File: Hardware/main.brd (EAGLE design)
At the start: 78.7 x 49.2 mm, 26 parts, among them IC3 MEGA128-A, K1 DS2-L2-12V, T1 IRML5202, T2 IRML5202, T3 IRML5202

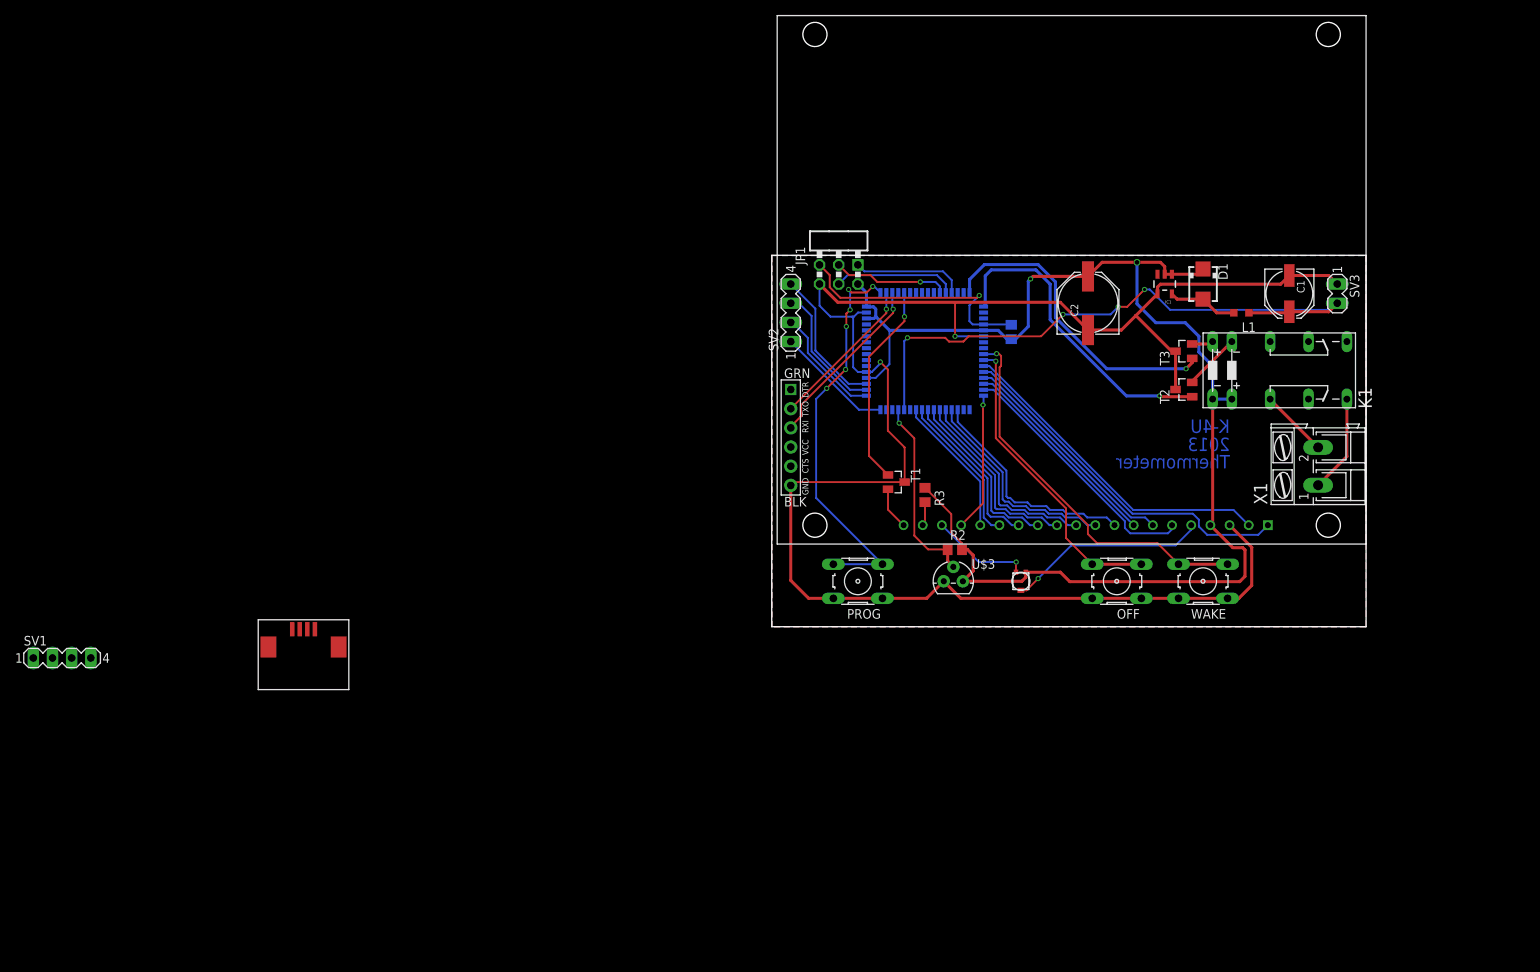
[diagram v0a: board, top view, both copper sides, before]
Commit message: Added a ds1307
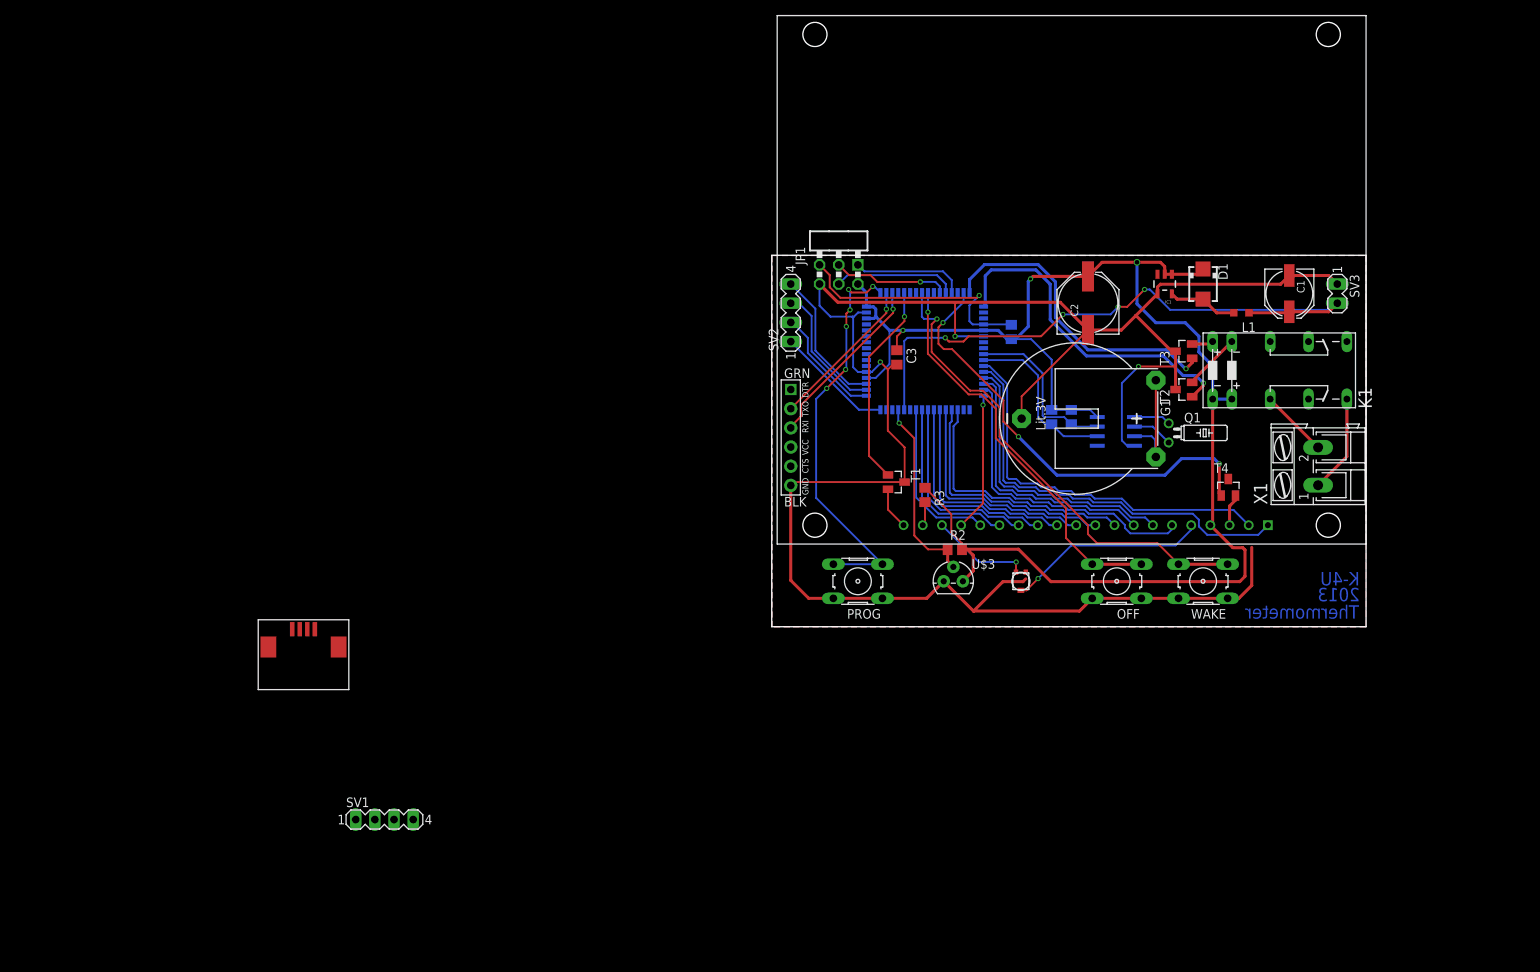
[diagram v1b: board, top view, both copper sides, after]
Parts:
- added C3: (no value), rcl:C0805
- added G1: CR2032H, battery:CR2032H
- added Q1: (no value), crystal:TC26H
- added R5, R6: 10K, rcl:R0805
- added T4: IRML5202, custom:SOT23
- added U1: DS1307ZN+, custom:SOIC127P600X175-8N
- moved SV1 47.8 mm to (-51.3, -25.2)
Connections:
- new net DISPLAY: IC3.15, T4.1
- new net N$23: T4.2, U$2.P$3
- new net N$24: G1.+, G1.+@1, U1.3
- new net N$26: Q1.1, U1.1
- new net N$27: Q1.2, U1.2
- new net SCL: IC3.25, R5.1, U1.7
- new net SDA: IC3.26, R6.1, U1.6
- net +5V: now also C3.1, R5.2, R6.2, U1.8; no longer R4.1
- net GND: now also C3.2, G1.-, R4.1, T4.3, U1.4; no longer U$2.P$3
- net N$10: now also IC3.8; no longer IC3.25
- net N$16: now also IC3.9; no longer IC3.26
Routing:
- net DISPLAY: track 0.00 -> 59.7 mm, vias 0 -> 3
- net GND: track 235.8 -> 276.2 mm, vias 2 -> 3
- net +5V: track 177.7 -> 200.7 mm, vias 2 -> 3
- net SDA: track 0.00 -> 22.5 mm
- net SCL: track 0.00 -> 22.3 mm
- net N$24: track 0.00 -> 15.4 mm
- net N$10: track 51.2 -> 63.8 mm
- net N$16: track 40.4 -> 52.5 mm
- net E: track 27.6 -> 35.3 mm
- net R/W: track 30.5 -> 37.9 mm
- net CS1: track 47.7 -> 55.1 mm
- net CS2: track 43.9 -> 51.1 mm
- net D/I: track 34.1 -> 41.1 mm
- net N$27: track 0.00 -> 5.41 mm
- net N$26: track 0.00 -> 4.88 mm
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
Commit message: Rotated the PCB, Added a button + LED
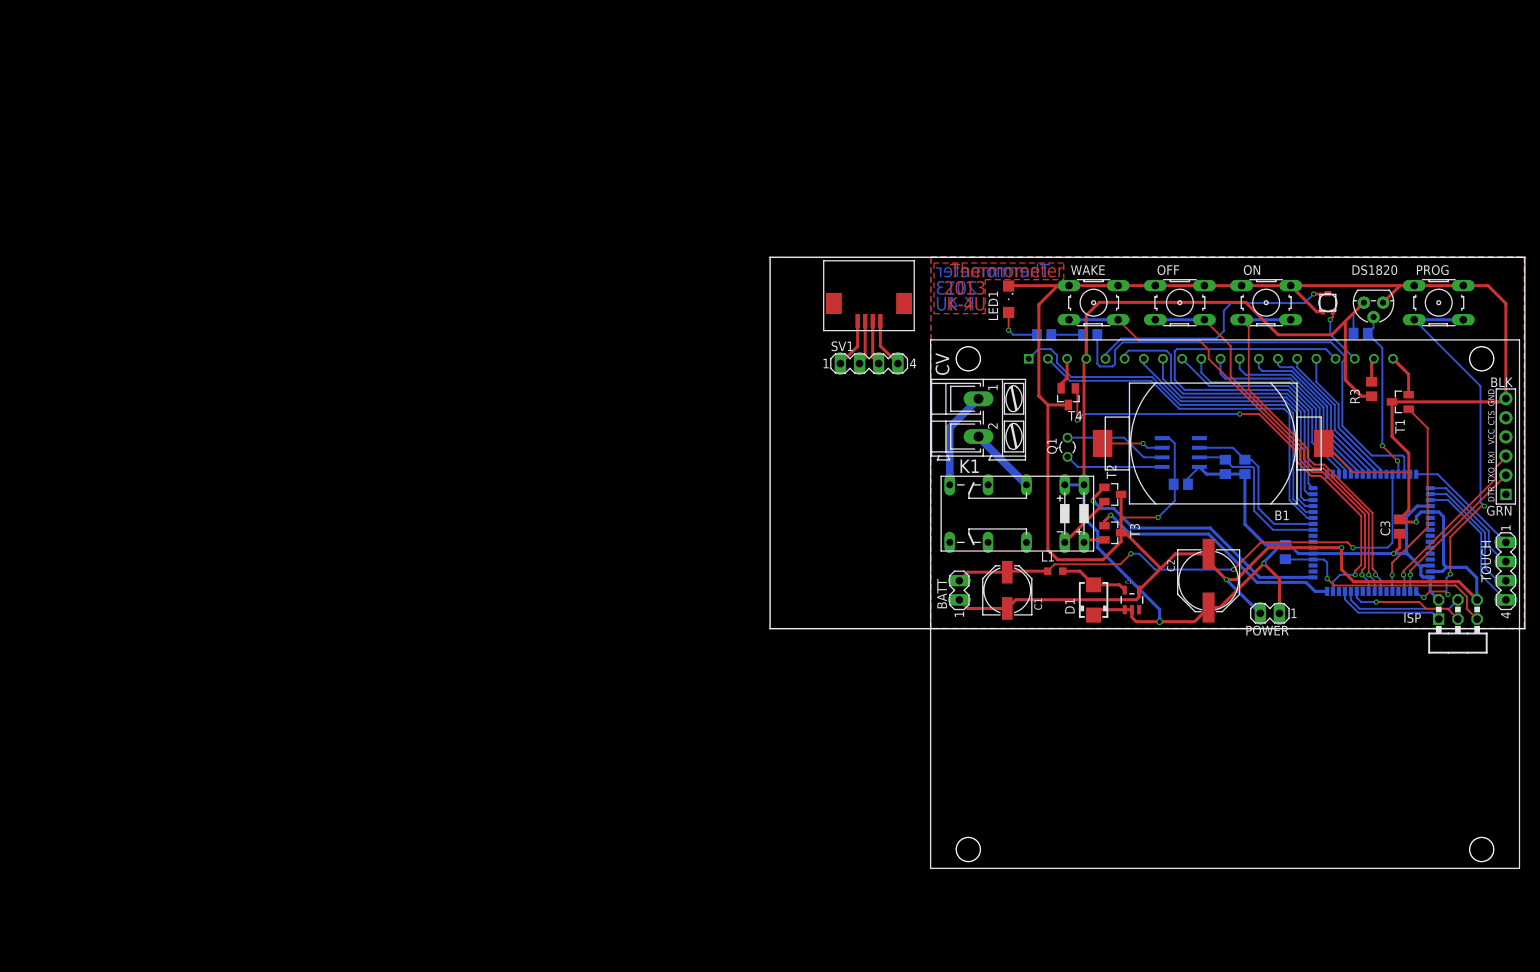
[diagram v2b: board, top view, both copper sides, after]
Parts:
- removed G1: CR2032H, battery:CR2032H
- removed JP1: AVR-ISP-6HORZ, avr-7:AVR-ISP-6R
- removed SV2: (no value), con-lstb:MA04-1
- removed SV3: (no value), con-lstb:MA02-1
- removed U$3: DS18B20, joep-custom:TO92
- removed X1: (no value), con-ptr500:AK300/2
- added B1: CR2032MULTICOMP, custom:CR2032
- added BATT, POWER: (no value), con-lstb:MA02-1
- added C4: (no value), rcl:C0805
- added CV: (no value), con-ptr500:AK300/2
- added DS1820: DS18B20, joep-custom:TO92
- added ISP: AVR-ISP-6HORZ, avr-7:AVR-ISP-6R
- added LED1: (no value), led:SML1206
- added ON: (no value), switch-omron:B3F-10XX
- added R7, R8: 150, rcl:R0805
- added TOUCH: (no value), con-lstb:MA04-1
- Q1: device crystal:TC26H -> crystal:TC26V
- moved U$2 126.8 mm to (21.1, -31.7), turned to 0 degrees
- moved JP2 94.7 mm to (97.3, 24.2), turned to 90 degrees
- moved SV1 88.1 mm to (12.9, 35.2)
- moved U$1 87.9 mm to (14.4, 40.8), turned to 180 degrees
- moved PROG 85.3 mm to (88.4, 43.2), turned to 0 degrees
- moved C3 70.3 mm to (83.2, 13.6), turned to 90 degrees
- moved T1 67.6 mm to (83.3, 30.1), turned to 90 degrees
- moved IC3 63.9 mm to (79.5, 12.8), turned to 90 degrees
- moved R2 60.9 mm to (78.0, 39.2), flipped to the bottom
- moved R3 60.8 mm to (79.5, 31.8), turned to 90 degrees
- moved R4 54.9 mm to (73.7, 43.2), turned to 0 degrees
- moved C1 54.2 mm to (31.2, 5.15), turned to 90 degrees
- moved R1 46.5 mm to (68.0, 10.2), turned to 270 degrees
- moved D1 44.3 mm to (42.6, 3.88), turned to 90 degrees
- moved L1 42.2 mm to (37.6, 7.69), turned to 0 degrees
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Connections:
- new net N$28: IC3.7, ON.3, ON.4
- new net N$29: LED1.A, R8.2
- new net N$30: IC3.46, R7.1
- new net N$31: R7.2, R8.1
- net !RESET: now also ISP.5; no longer JP1.5
- net +5V: now also C4.1, DS1820.3, ISP.2, POWER.1; no longer JP1.2, U$3.3
- net DS18B20: now also DS1820.2; no longer U$3.2
- net GND: now also B1.NEG, BATT.1, C4.2, DS1820.1, ISP.6, LED1.C, ON.1, ON.2, POWER.2; no longer G1.-, JP1.6, SV3.1, U$3.1
- net MISO: now also ISP.1; no longer JP1.1
- net MOSI: now also ISP.4; no longer JP1.4
- net N$10: now also IC3.9; no longer IC3.8
- net N$16: now also IC3.8; no longer IC3.9
- net N$17: now also CV.2; no longer X1.2
- net N$18: now also CV.1; no longer X1.1
- net N$19: now also TOUCH.4; no longer SV2.4
- net N$20: now also TOUCH.3; no longer SV2.3
- net N$21: now also TOUCH.2; no longer SV2.2
- net N$22: now also TOUCH.1; no longer SV2.1
- net N$24: now also B1.POS; no longer G1.+, G1.+@1
- net SCK: now also ISP.3; no longer JP1.3
- net V+: now also BATT.2; no longer SV3.2
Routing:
- net N$30: track 0.00 -> 61.5 mm
- net GND: track 276.2 -> 331.8 mm, vias 3 -> 4
- net N$28: track 0.00 -> 50.9 mm, vias 0 -> 1
- net RST: track 18.4 -> 55.7 mm, vias 1 -> 0
- net V+: track 83.4 -> 70.9 mm, vias 4 -> 3
- net R_S: track 44.8 -> 35.7 mm
- net N$13: track 26.5 -> 35.0 mm
- net N$27: track 5.41 -> 13.6 mm
- net N$26: track 4.88 -> 13.1 mm
- net N$24: track 15.4 -> 8.12 mm, vias 0 -> 1
- net R_R: track 41.4 -> 34.6 mm
- net N$3: track 0.00 -> 6.58 mm
- net N$6: track 0.00 -> 6.56 mm
- net N$29: track 0.00 -> 6.35 mm, vias 0 -> 1
- net N$4: track 0.00 -> 5.94 mm
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- added copper zone on layer 1, net N$32
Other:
- board size 78.7 x 49.2 mm -> 100 x 49.2 mm

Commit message: Partially working firmware. It's just a test
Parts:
- added R9: 10K, rcl:R0805
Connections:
- new net CV_ON: IC3.14, K1.S2, R9.2
- net +5V: now also K1.P2
- net GND: now also R9.1
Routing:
- net CV_ON: track 0.00 -> 56.8 mm, vias 0 -> 2
- net +5V: track 204.4 -> 213.5 mm
- net GND: track 331.8 -> 339.6 mm
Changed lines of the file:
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@@
 <element name="C4" library="rcl" package="C0805" value="" x="54.2" y="19.2" rot="MR0"/>
 <element name="POWER" library="con-lstb" package="MA02-1" value="" x="66" y="2.1" rot="R180"/>
+<element name="R9" library="rcl" package="R0805" value="10K" x="69.9" y="3.2" rot="MR90"/>
 </elements>
 <signals>
@@
 <wire x1="82.2359" y1="20.5297" x2="82.2359" y2="11.4359" width="0.254" layer="16"/>
 <wire x1="82.2359" y1="11.4359" x2="81.6" y2="10.8" width="0.254" layer="16"/>
-<via x="61.2" y="7.9" extent="1-16" drill="0.4"/>
-<wire x1="64.8" y1="11.5" x2="61.2" y2="7.9" width="0.254" layer="1"/>
-<wire x1="61.2" y1="7.9" x2="50.8" y2="7.9" width="0.254" layer="16"/>
-<wire x1="76.3" y1="11.5" x2="64.8" y2="11.5" width="0.254" layer="1"/>
-<wire x1="50.8" y1="7.9" x2="48.7" y2="10" width="0.254" layer="16"/>
+<wire x1="76.3" y1="11.5" x2="61.4" y2="11.5" width="0.254" layer="1"/>
 <wire x1="48.7" y1="10" x2="47.6" y2="10" width="0.254" layer="16"/>
 <via x="47.6" y="10" extent="1-16" drill="0.4"/>
@@
 <via x="77" y="10.8" extent="1-16" drill="0.4"/>
 <wire x1="77" y1="10.8" x2="81.6" y2="10.8" width="0.254" layer="16"/>
+<wire x1="48.7" y1="10" x2="50.2" y2="11.5" width="0.254" layer="16"/>
+<wire x1="50.2" y1="11.5" x2="55.5" y2="11.5" width="0.254" layer="16"/>
+<via x="55.5" y="11.5" extent="1-16" drill="0.4"/>
+<wire x1="55.5" y1="11.5" x2="57.2" y2="13.2" width="0.254" layer="1"/>
+<wire x1="57.2" y1="13.2" x2="59.7" y2="13.2" width="0.254" layer="1"/>
+<wire x1="59.7" y1="13.2" x2="61.4" y2="11.5" width="0.254" layer="1"/>
 </signal>
 <signal name="N$1">
@@
 <wire x1="77.1" y1="6.3" x2="91.03" y2="6.3" width="0.4064" layer="1"/>
 <wire x1="61.56" y1="6.56" x2="60.24" y2="6.56" width="0.4064" layer="1"/>
-<wire x1="59.45" y1="7.35" x2="58" y2="8.8" width="0.4064" layer="1"/>
+<wire x1="60.24" y1="6.56" x2="58" y2="8.8" width="0.4064" layer="1"/>
 <wire x1="58" y1="8.8" x2="58" y2="9.86" width="0.4064" layer="1"/>
 <wire x1="58" y1="9.86" x2="57.89" y2="9.97" width="0.4064" layer="1"/>
@@
 <wire x1="64.7" y1="2.1" x2="60.24" y2="6.56" width="0.4064" layer="16"/>
 <via x="60.24" y="6.56" extent="1-16" drill="0.4"/>
-<wire x1="60.24" y1="6.56" x2="59.45" y2="7.35" width="0.4064" layer="1"/>
+<contactref element="R9" pad="1"/>
+<wire x1="69.9" y1="2.25" x2="67.55" y2="4.6" width="0.254" layer="16"/>
+<wire x1="67.55" y1="4.6" x2="66.2" y2="4.6" width="0.254" layer="16"/>
+<wire x1="66.2" y1="4.6" x2="64.73" y2="3.13" width="0.254" layer="16"/>
+<wire x1="64.73" y1="3.13" x2="64.73" y2="2.1" width="0.254" layer="16"/>
 </signal>
 <signal name="+5V">
@@
 <wire x1="41.68" y1="35.82" x2="41.38" y2="35.52" width="0.4064" layer="1"/>
 <wire x1="41.38" y1="35.52" x2="41.38" y2="19.12" width="0.4064" layer="1"/>
-<wire x1="41.38" y1="19.12" x2="41.38" y2="14.72" width="0.4064" layer="16"/>
+<wire x1="41.38" y1="19.12" x2="41.38" y2="15.2" width="0.4064" layer="16"/>
+<wire x1="41.38" y1="15.2" x2="41.38" y2="14.72" width="0.4064" layer="16"/>
 <wire x1="41.38" y1="14.72" x2="43.2" y2="12.9" width="0.4064" layer="16"/>
 <wire x1="43.2" y1="12.9" x2="43.2" y2="10.8" width="0.4064" layer="16"/>
@@
 <wire x1="43.2" y1="10.8" x2="51.4" y2="2.6" width="0.4064" layer="16"/>
 <wire x1="51.4" y1="2.6" x2="51.4" y2="1" width="0.4064" layer="16"/>
+<contactref element="K1" pad="P2"/>
+<wire x1="33.76" y1="11.5" x2="37.46" y2="15.2" width="0.254" layer="16"/>
+<wire x1="37.46" y1="15.2" x2="41.38" y2="15.2" width="0.254" layer="16"/>
 </signal>
 <signal name="D0">
@@
 <wire x1="49.765" y1="24.035" x2="51.7362" y2="24.035" width="0.254" layer="16"/>
 </signal>
+<signal name="CV_ON">
+<contactref element="K1" pad="S2"/>
+<contactref element="R9" pad="2"/>
+<contactref element="IC3" pad="14"/>
+<wire x1="69.9" y1="4.15" x2="70.35" y2="3.7" width="0.254" layer="16"/>
+<wire x1="70.35" y1="3.7" x2="74.7" y2="3.7" width="0.254" layer="16"/>
+<wire x1="74.7" y1="3.7" x2="75.1493" y2="4.1493" width="0.254" layer="16"/>
+<wire x1="75.1493" y1="4.1493" x2="75.1493" y2="5.0103" width="0.254" layer="16"/>
+<wire x1="69.9" y1="4.15" x2="68.65" y2="5.4" width="0.254" layer="16"/>
+<wire x1="68.65" y1="5.4" x2="63.9" y2="5.4" width="0.254" layer="16"/>
+<wire x1="63.9" y1="5.4" x2="60.4" y2="8.9" width="0.254" layer="16"/>
+<wire x1="60.4" y1="8.9" x2="49.1" y2="8.9" width="0.254" layer="16"/>
+<via x="49.1" y="8.9" extent="1-16" drill="0.4"/>
+<wire x1="49.1" y1="8.9" x2="47.9" y2="7.7" width="0.254" layer="1"/>
+<wire x1="47.9" y1="7.7" x2="43.6" y2="7.7" width="0.254" layer="1"/>
+<via x="43.6" y="7.7" extent="1-16" drill="0.4"/>
+<wire x1="43.6" y1="7.7" x2="27.4" y2="7.7" width="0.254" layer="16"/>
+<wire x1="27.4" y1="7.7" x2="23.6" y2="11.5" width="0.254" layer="16"/>
+</signal>
 </signals>
